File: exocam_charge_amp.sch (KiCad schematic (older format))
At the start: 8 parts, among them J1 dupont2x1, U1 TLV2771CDBVT

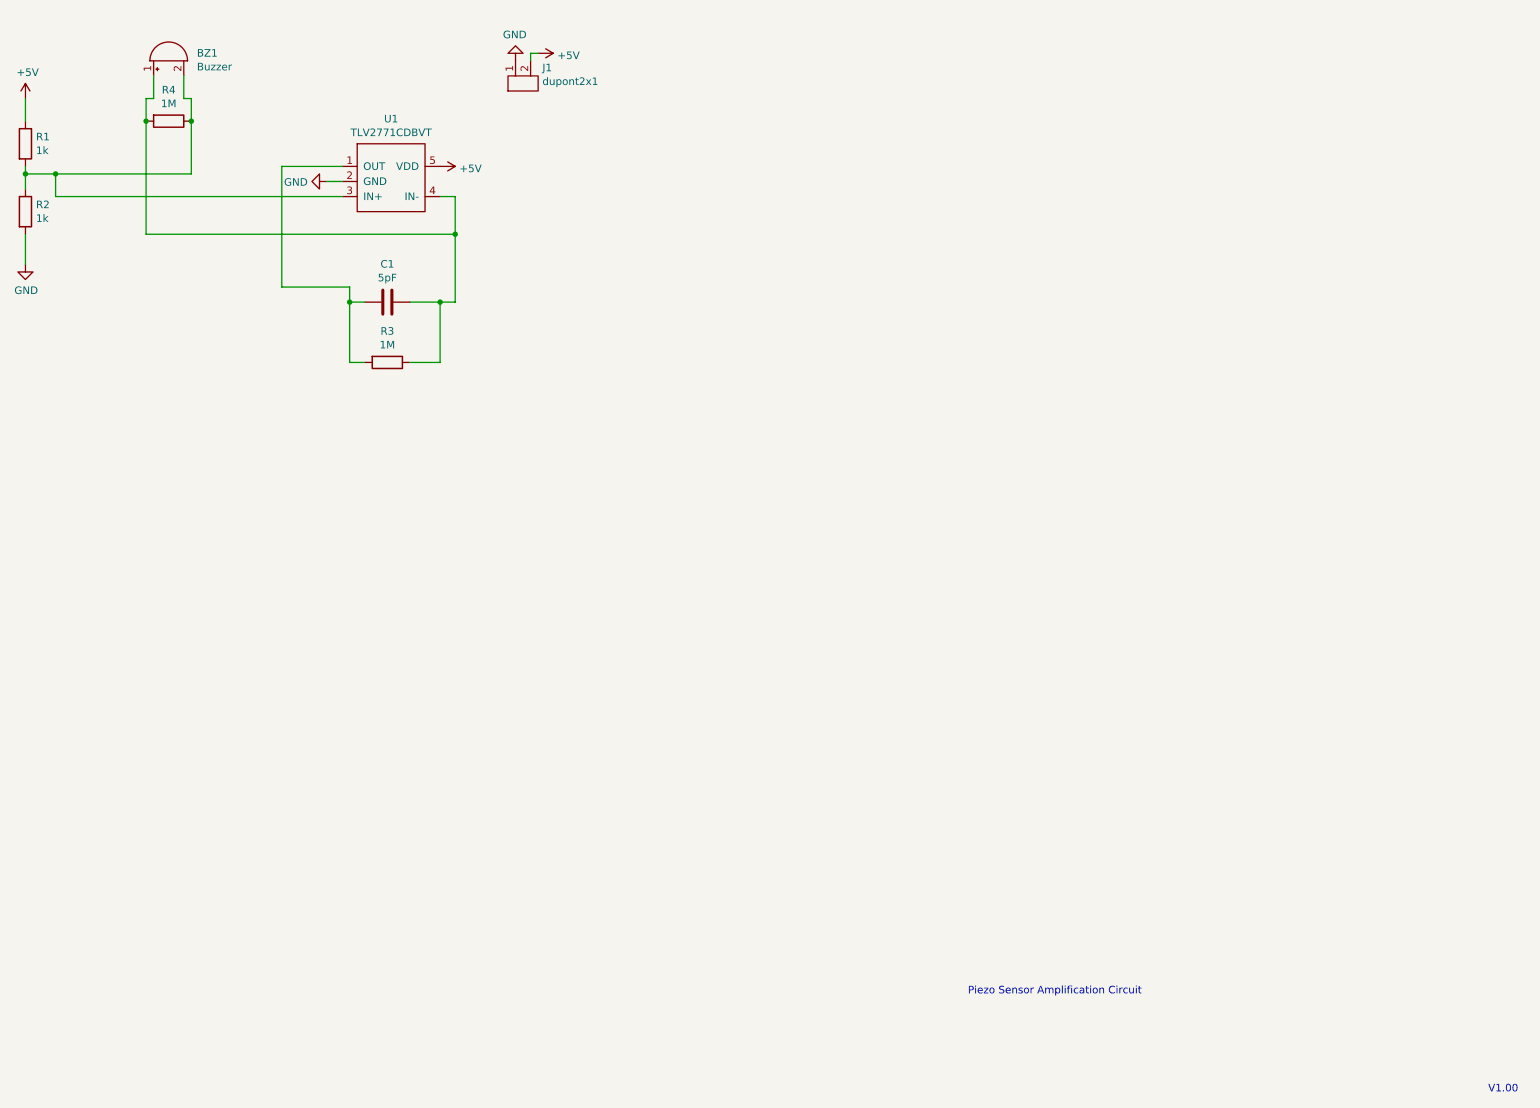
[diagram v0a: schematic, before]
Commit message: added step and updated to have screw mounts for the board
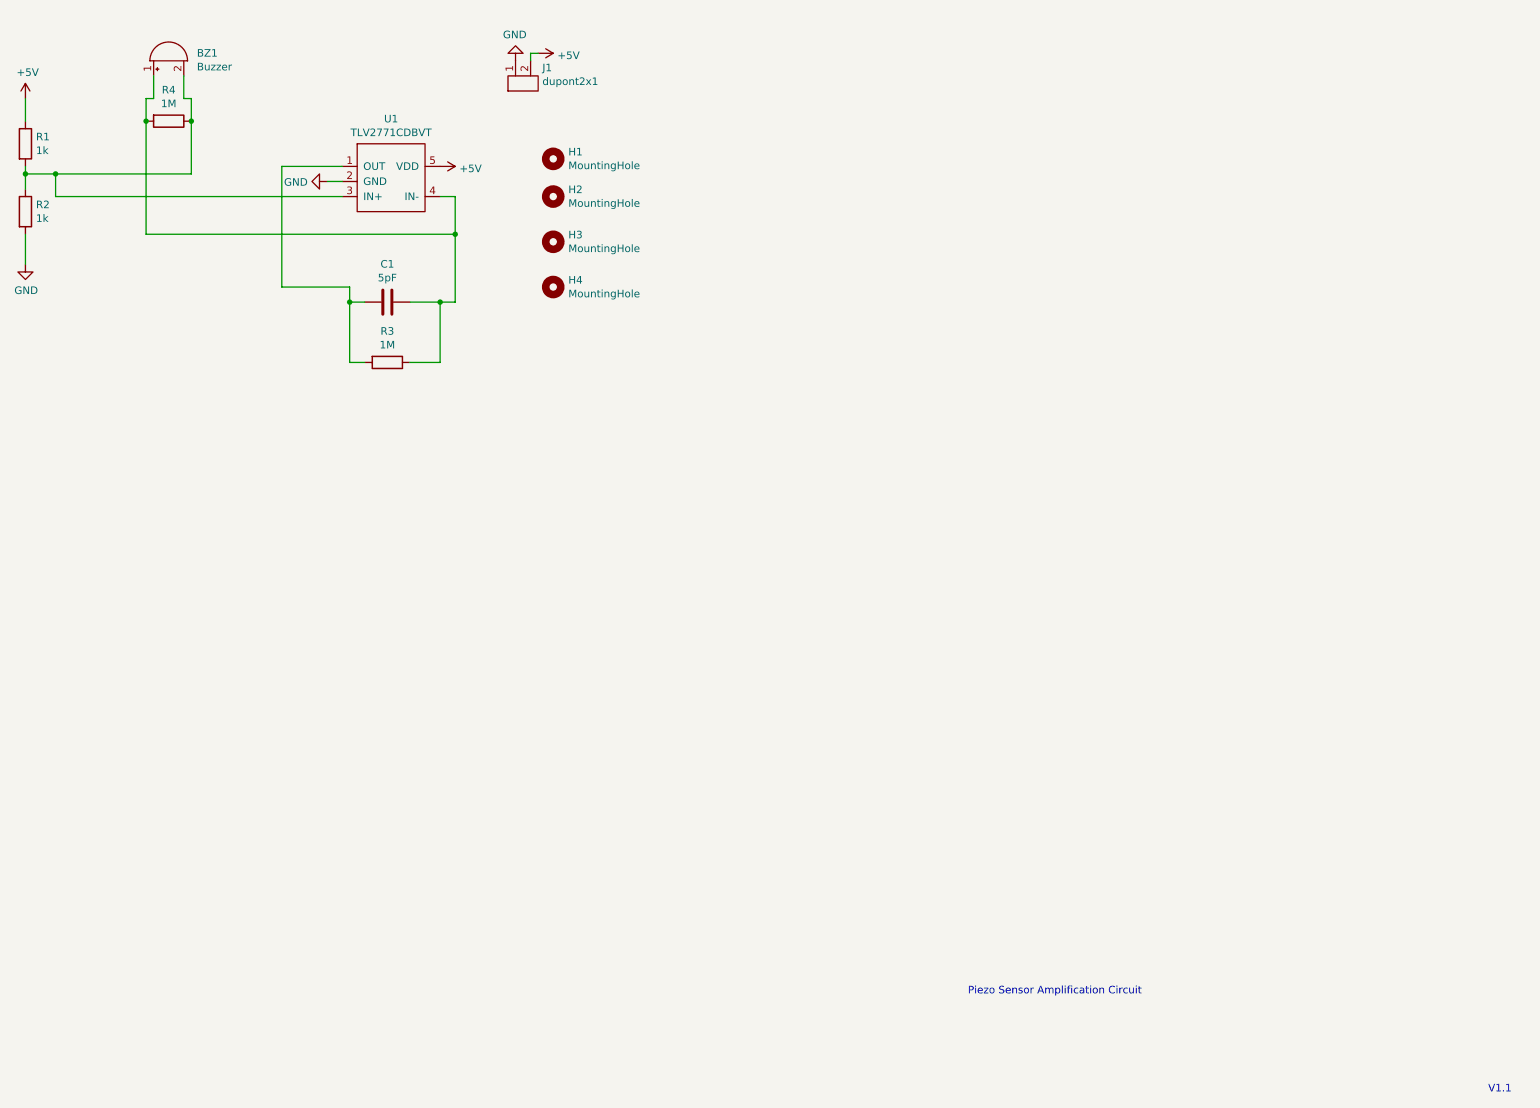
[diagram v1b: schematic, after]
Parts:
- added H1, H2, H3, H4: MountingHole, exocam_charge_amp:mount_hole_2.5mm, symbol Mechanical:MountingHole
- J1: footprint (none) -> exocam_charge_amp:dupont2x1
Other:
- note added: "V1.1\n"
- note removed: "V1.00\n"
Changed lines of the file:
@@
 Piezo Sensor Amplification Circuit
 Text Notes 10600 7650 0    50   ~ 0
-V1.00\n
+V1.1\n
 $Comp
 L exocam_charge_amp:TLV2771CDBVT U1
@@
 F 0 "J1" V 4154 672 50  0000 R CNN
 F 1 "dupont2x1" V 4063 672 50  0000 R CNN
-F 2 "" H 4050 1050 50  0001 C CNN
+F 2 "exocam_charge_amp:dupont2x1" H 4050 1050 50  0001 C CNN
 F 3 "" H 4050 1050 50  0001 C CNN
 	1    4100 900
@@
 $EndComp
 $Comp
-L power:GND #PWR?
+L power:GND #PWR0105
 U 1 1 60B84C12
 P 4150 800
-F 0 "#PWR?" H 4150 550 50  0001 C CNN
+F 0 "#PWR0105" H 4150 550 50  0001 C CNN
 F 1 "GND" H 4155 627 50  0000 C CNN
 F 2 "" H 4150 800 50  0001 C CNN
@@
 $EndComp
 $Comp
-L power:+5V #PWR?
+L power:+5V #PWR0106
 U 1 1 60B84E19
 P 4300 750
-F 0 "#PWR?" H 4300 600 50  0001 C CNN
+F 0 "#PWR0106" H 4300 600 50  0001 C CNN
 F 1 "+5V" V 4315 878 50  0000 L CNN
 F 2 "" H 4300 750 50  0001 C CNN
@@
 Wire Wire Line
 	1950 1050 1950 900
+$Comp
+L Mechanical:MountingHole H1
+U 1 1 60B97329
+P 4400 1450
+F 0 "H1" H 4500 1496 50  0000 L CNN
+F 1 "MountingHole" H 4500 1405 50  0000 L CNN
+F 2 "exocam_charge_amp:mount_hole_2.5mm" H 4400 1450 50  0001 C CNN
+F 3 "~" H 4400 1450 50  0001 C CNN
+	1    4400 1450
+	1    0    0    -1
+$EndComp
+$Comp
+L Mechanical:MountingHole H2
+U 1 1 60B9898F
+P 4400 1700
+F 0 "H2" H 4500 1746 50  0000 L CNN
+F 1 "MountingHole" H 4500 1655 50  0000 L CNN
+F 2 "exocam_charge_amp:mount_hole_2.5mm" H 4400 1700 50  0001 C CNN
+F 3 "~" H 4400 1700 50  0001 C CNN
+	1    4400 1700
+	1    0    0    -1
+$EndComp
+$Comp
+L Mechanical:MountingHole H3
+U 1 1 60B99095
+P 4400 2000
+F 0 "H3" H 4500 2046 50  0000 L CNN
+F 1 "MountingHole" H 4500 1955 50  0000 L CNN
+F 2 "exocam_charge_amp:mount_hole_2.5mm" H 4400 2000 50  0001 C CNN
+F 3 "~" H 4400 2000 50  0001 C CNN
+	1    4400 2000
+	1    0    0    -1
+$EndComp
+$Comp
+L Mechanical:MountingHole H4
+U 1 1 60B99959
+P 4400 2300
+F 0 "H4" H 4500 2346 50  0000 L CNN
+F 1 "MountingHole" H 4500 2255 50  0000 L CNN
+F 2 "exocam_charge_amp:mount_hole_2.5mm" H 4400 2300 50  0001 C CNN
+F 3 "~" H 4400 2300 50  0001 C CNN
+	1    4400 2300
+	1    0    0    -1
+$EndComp
 $EndSCHEMATC

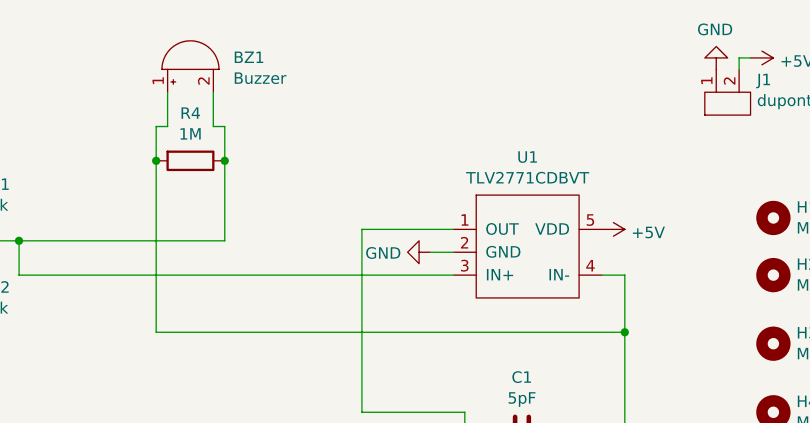
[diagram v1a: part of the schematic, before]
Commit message: added output terminals
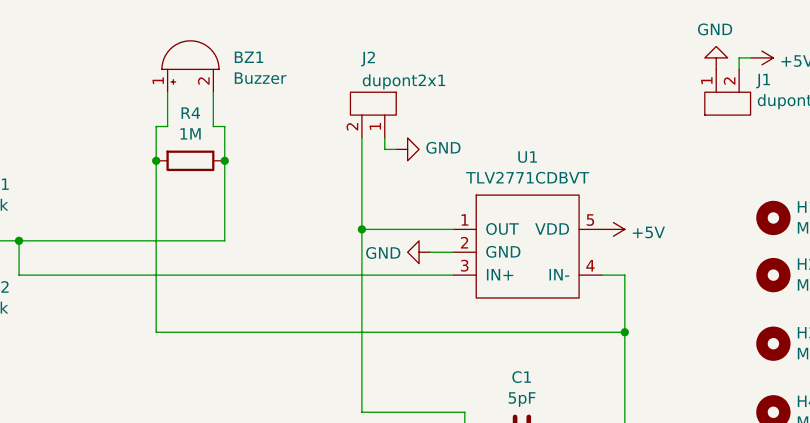
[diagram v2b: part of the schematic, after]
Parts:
- added J2: dupont2x1, exocam_charge_amp:dupont2x1, symbol exocam_charge_amp:dupont2x1
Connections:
- net GND: now also J2.1
- net at C1.2, R3.2, U1.1 (OUT): now also J2.2
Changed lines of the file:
@@
 	1    0    0    -1
 $EndComp
+$Comp
+L exocam_charge_amp:dupont2x1 J2
+U 1 1 60BB220E
+P 2750 1000
+F 0 "J2" V 2500 850 50  0000 L CNN
+F 1 "dupont2x1" V 2600 850 50  0000 L CNN
+F 2 "exocam_charge_amp:dupont2x1" H 2700 1150 50  0001 C CNN
+F 3 "" H 2700 1150 50  0001 C CNN
+	1    2750 1000
+	0    1    1    0
+$EndComp
+$Comp
+L power:GND #PWR?
+U 1 1 60BB5C21
+P 2750 1150
+F 0 "#PWR?" H 2750 900 50  0001 C CNN
+F 1 "GND" V 2755 1022 50  0000 R CNN
+F 2 "" H 2750 1150 50  0001 C CNN
+F 3 "" H 2750 1150 50  0001 C CNN
+	1    2750 1150
+	0    -1   -1   0
+$EndComp
+Wire Wire Line
+	2750 1150 2700 1150
+Wire Wire Line
+	2700 1150 2700 1100
+Wire Wire Line
+	2600 1100 2600 1500
+Connection ~ 2600 1500
 $EndSCHEMATC

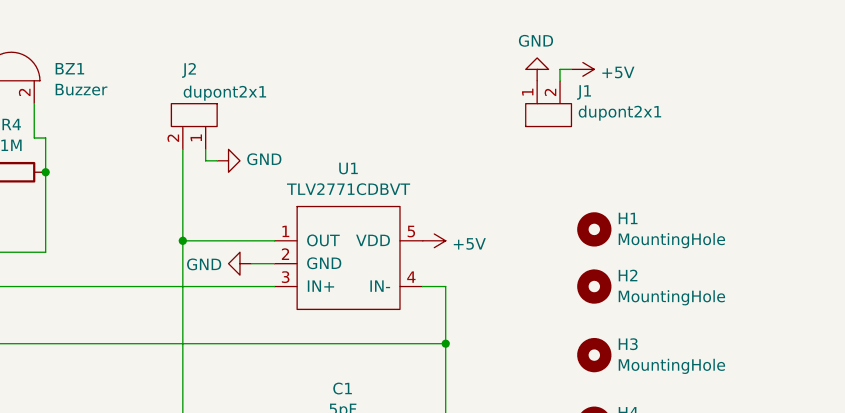
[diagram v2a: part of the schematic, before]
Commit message: updated pcb to be the new hole pattern on the shoulder side
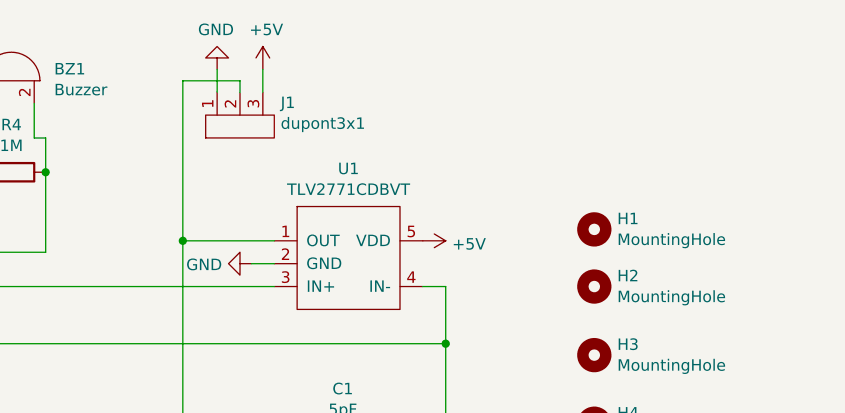
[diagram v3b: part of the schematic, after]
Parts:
- removed J1, J2: dupont2x1, exocam_charge_amp:dupont2x1, symbol exocam_charge_amp:dupont2x1
- added J1: dupont3x1, exocam_charge_amp:dupont3x1, symbol exocam_charge_amp:dupont3x1
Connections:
- net +5V: now also J1.3
- net GND: now also J1.1
- net at C1.2, R3.2, U1.1 (OUT): now also J1.2
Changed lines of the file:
@@
 	0    1    1    0
 $EndComp
-$Comp
-L exocam_charge_amp:dupont2x1 J1
-U 1 1 60B80DC6
-P 4100 900
-F 0 "J1" V 4154 672 50  0000 R CNN
-F 1 "dupont2x1" V 4063 672 50  0000 R CNN
-F 2 "exocam_charge_amp:dupont2x1" H 4050 1050 50  0001 C CNN
-F 3 "" H 4050 1050 50  0001 C CNN
-	1    4100 900
-	0    -1   -1   0
-$EndComp
-$Comp
-L power:GND #PWR0105
-U 1 1 60B84C12
-P 4150 800
-F 0 "#PWR0105" H 4150 550 50  0001 C CNN
-F 1 "GND" H 4155 627 50  0000 C CNN
-F 2 "" H 4150 800 50  0001 C CNN
-F 3 "" H 4150 800 50  0001 C CNN
-	1    4150 800
-	-1   0    0    1
-$EndComp
-$Comp
-L power:+5V #PWR0106
-U 1 1 60B84E19
-P 4300 750
-F 0 "#PWR0106" H 4300 600 50  0001 C CNN
-F 1 "+5V" V 4315 878 50  0000 L CNN
-F 2 "" H 4300 750 50  0001 C CNN
-F 3 "" H 4300 750 50  0001 C CNN
-	1    4300 750
-	0    1    1    0
-$EndComp
-Wire Wire Line
-	4250 750  4300 750
-Wire Wire Line
-	4250 800  4250 750
 Wire Wire Line
 	1750 1050 1750 900
@@
 $EndComp
 $Comp
-L exocam_charge_amp:dupont2x1 J2
-U 1 1 60BB220E
-P 2750 1000
-F 0 "J2" V 2500 850 50  0000 L CNN
-F 1 "dupont2x1" V 2600 850 50  0000 L CNN
-F 2 "exocam_charge_amp:dupont2x1" H 2700 1150 50  0001 C CNN
-F 3 "" H 2700 1150 50  0001 C CNN
-	1    2750 1000
-	0    1    1    0
+L exocam_charge_amp:dupont3x1 J1
+U 1 1 60DCA11E
+P 2700 950
+F 0 "J1" V 2754 622 50  0000 R CNN
+F 1 "dupont3x1" V 2663 622 50  0000 R CNN
+F 2 "exocam_charge_amp:dupont3x1" H 2650 1100 50  0001 C CNN
+F 3 "" H 2650 1100 50  0001 C CNN
+	1    2700 950
+	0    -1   -1   0
 $EndComp
 $Comp
 L power:GND #PWR?
-U 1 1 60BB5C21
-P 2750 1150
-F 0 "#PWR?" H 2750 900 50  0001 C CNN
-F 1 "GND" V 2755 1022 50  0000 R CNN
-F 2 "" H 2750 1150 50  0001 C CNN
-F 3 "" H 2750 1150 50  0001 C CNN
-	1    2750 1150
-	0    -1   -1   0
+U 1 1 60DCCF64
+P 2750 750
+F 0 "#PWR?" H 2750 500 50  0001 C CNN
+F 1 "GND" H 2755 577 50  0000 C CNN
+F 2 "" H 2750 750 50  0001 C CNN
+F 3 "" H 2750 750 50  0001 C CNN
+	1    2750 750
+	-1   0    0    1
 $EndComp
 Wire Wire Line
-	2750 1150 2700 1150
+	2750 850  2750 750
+$Comp
+L power:+5V #PWR?
+U 1 1 60DD0686
+P 2950 750
+F 0 "#PWR?" H 2950 600 50  0001 C CNN
+F 1 "+5V" H 2965 923 50  0000 C CNN
+F 2 "" H 2950 750 50  0001 C CNN
+F 3 "" H 2950 750 50  0001 C CNN
+	1    2950 750
+	1    0    0    -1
+$EndComp
 Wire Wire Line
-	2700 1150 2700 1100
+	2950 850  2950 750
 Wire Wire Line
-	2600 1100 2600 1500
+	2850 850  2850 800
+Wire Wire Line
+	2600 1500 2600 800
+Wire Wire Line
+	2600 800  2850 800
 Connection ~ 2600 1500
 $EndSCHEMATC

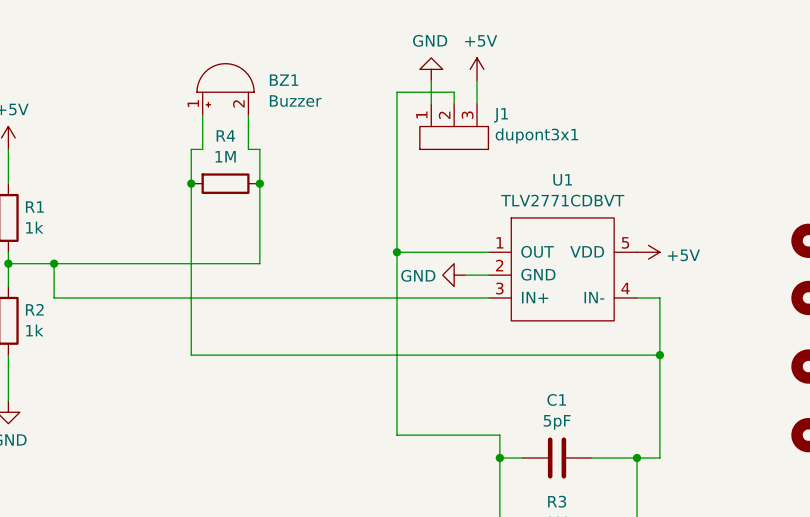
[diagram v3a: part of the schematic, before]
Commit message: modify board to be the two way amplification stage for higher range of outputs
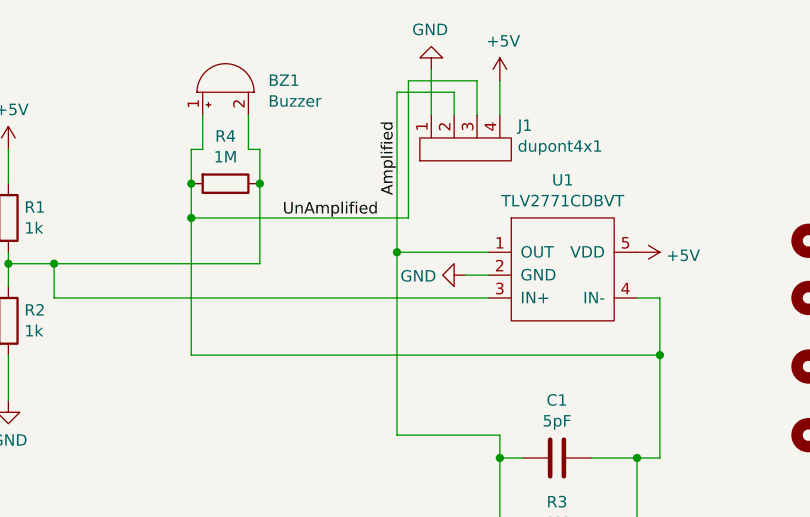
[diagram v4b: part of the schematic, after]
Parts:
- removed J1: dupont3x1, exocam_charge_amp:dupont3x1, symbol exocam_charge_amp:dupont3x1
- added J1: dupont4x1, exocam_charge_amp:dupont4x1, symbol exocam_charge_amp:dupont4x1
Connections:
- net +5V: now also J1.4
- net GND: now also J1.1
- net UnAmplified: now reaches BZ1.1 (-), C1.1, R3.1, R4.2, U1.4 (IN-)
- net UnAmplified: now also J1.3
- net Amplified: now reaches C1.2, R3.2, U1.1 (OUT)
- net Amplified: now also J1.2
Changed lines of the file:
@@
 	1700 1950 3750 1950
 Wire Wire Line
-	1700 1200 1700 1950
+	1700 1200 1700 1350
 Connection ~ 3750 1950
 Wire Wire Line
@@
 $EndComp
 $Comp
-L exocam_charge_amp:dupont3x1 J1
-U 1 1 60DCA11E
-P 2700 950
-F 0 "J1" V 2754 622 50  0000 R CNN
-F 1 "dupont3x1" V 2663 622 50  0000 R CNN
-F 2 "exocam_charge_amp:dupont3x1" H 2650 1100 50  0001 C CNN
-F 3 "" H 2650 1100 50  0001 C CNN
-	1    2700 950
-	0    -1   -1   0
+L power:GND #PWR0105
+U 1 1 60DCCF64
+P 2750 700
+F 0 "#PWR0105" H 2750 450 50  0001 C CNN
+F 1 "GND" H 2755 527 50  0000 C CNN
+F 2 "" H 2750 700 50  0001 C CNN
+F 3 "" H 2750 700 50  0001 C CNN
+	1    2750 700
+	-1   0    0    1
 $EndComp
 $Comp
-L power:GND #PWR?
-U 1 1 60DCCF64
-P 2750 750
-F 0 "#PWR?" H 2750 500 50  0001 C CNN
-F 1 "GND" H 2755 577 50  0000 C CNN
-F 2 "" H 2750 750 50  0001 C CNN
-F 3 "" H 2750 750 50  0001 C CNN
-	1    2750 750
-	-1   0    0    1
-$EndComp
-Wire Wire Line
-	2750 850  2750 750
-$Comp
-L power:+5V #PWR?
+L power:+5V #PWR0106
 U 1 1 60DD0686
-P 2950 750
-F 0 "#PWR?" H 2950 600 50  0001 C CNN
-F 1 "+5V" H 2965 923 50  0000 C CNN
-F 2 "" H 2950 750 50  0001 C CNN
-F 3 "" H 2950 750 50  0001 C CNN
-	1    2950 750
+P 3050 750
+F 0 "#PWR0106" H 3050 600 50  0001 C CNN
+F 1 "+5V" H 3065 923 50  0000 C CNN
+F 2 "" H 3050 750 50  0001 C CNN
+F 3 "" H 3050 750 50  0001 C CNN
+	1    3050 750
 	1    0    0    -1
 $EndComp
-Wire Wire Line
-	2950 850  2950 750
-Wire Wire Line
-	2850 850  2850 800
 Wire Wire Line
 	2600 1500 2600 800
@@
 	2600 800  2850 800
 Connection ~ 2600 1500
+$Comp
+L exocam_charge_amp:dupont4x1 J1
+U 1 1 60DF5917
+P 2700 1000
+F 0 "J1" V 2754 572 50  0000 R CNN
+F 1 "dupont4x1" V 2663 572 50  0000 R CNN
+F 2 "exocam_charge_amp:dupont4x1" H 2650 1150 50  0001 C CNN
+F 3 "" H 2650 1150 50  0001 C CNN
+	1    2700 1000
+	0    -1   -1   0
+$EndComp
+Wire Wire Line
+	3050 900  3050 750
+Wire Wire Line
+	2850 800  2850 900
+Wire Wire Line
+	2750 700  2750 900
+Wire Wire Line
+	1700 1350 2650 1350
+Wire Wire Line
+	2650 1350 2650 750
+Wire Wire Line
+	2650 750  2950 750
+Wire Wire Line
+	2950 750  2950 900
+Connection ~ 1700 1350
+Wire Wire Line
+	1700 1350 1700 1950
+Text Label 2100 1350 0    50   ~ 0
+UnAmplified
+Text Label 2600 1250 1    50   ~ 0
+Amplified
 $EndSCHEMATC

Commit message: updated so that vertical distance is correct for the holes
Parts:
- BZ1: symbol Device:Buzzer -> exocam_charge_amp-rescue:Buzzer-Device
- C1: symbol Device:C -> exocam_charge_amp-rescue:C-Device
- H1, H2, H3, H4: symbol Mechanical:MountingHole -> exocam_charge_amp-rescue:MountingHole-Mechanical
- R1, R2, R3, R4: symbol Device:R -> exocam_charge_amp-rescue:R-Device
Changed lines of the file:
@@
 $EndDescr
 $Comp
-L power:+5V #PWR0101
+L exocam_charge_amp-rescue:+5V-power #PWR0101
 U 1 1 60AC4579
 P 900 1050
@@
 $EndComp
 $Comp
-L Device:R R1
+L exocam_charge_amp-rescue:R-Device R1
 U 1 1 60AC52F9
 P 900 1350
@@
 $EndComp
 $Comp
-L Device:R R2
+L exocam_charge_amp-rescue:R-Device R2
 U 1 1 60AC57F6
 P 900 1800
@@
 	900  1950 900  2150
 $Comp
-L power:GND #PWR0102
+L exocam_charge_amp-rescue:GND-power #PWR0102
 U 1 1 60AC7448
 P 900 2150
@@
 $EndComp
 $Comp
-L Device:C C1
+L exocam_charge_amp-rescue:C-Device C1
 U 1 1 60AC9C31
 P 3300 2400
@@
 	3450 2400 3650 2400
 $Comp
-L Device:R R3
+L exocam_charge_amp-rescue:R-Device R3
 U 1 1 60ACB29B
 P 3300 2800
@@
 	3650 2800 3650 2400
 $Comp
-L Device:Buzzer BZ1
+L exocam_charge_amp-rescue:Buzzer-Device BZ1
 U 1 1 60AEB9E7
 P 1850 800
@@
 $EndComp
 $Comp
-L Device:R R4
+L exocam_charge_amp-rescue:R-Device R4
 U 1 1 60AECA35
 P 1850 1200
@@
 $EndComp
 $Comp
-L power:GND #PWR0103
+L exocam_charge_amp-rescue:GND-power #PWR0103
 U 1 1 60B68AE8
 P 2900 1600
@@
 	3750 1950 3750 2400
 $Comp
-L power:+5V #PWR0104
+L exocam_charge_amp-rescue:+5V-power #PWR0104
 U 1 1 60B6BDDA
 P 3650 1500
@@
 	1950 1050 1950 900
 $Comp
-L Mechanical:MountingHole H1
+L exocam_charge_amp-rescue:MountingHole-Mechanical H1
 U 1 1 60B97329
 P 4400 1450
@@
 $EndComp
 $Comp
-L Mechanical:MountingHole H2
+L exocam_charge_amp-rescue:MountingHole-Mechanical H2
 U 1 1 60B9898F
 P 4400 1700
@@
 $EndComp
 $Comp
-L Mechanical:MountingHole H3
+L exocam_charge_amp-rescue:MountingHole-Mechanical H3
 U 1 1 60B99095
 P 4400 2000
@@
 $EndComp
 $Comp
-L Mechanical:MountingHole H4
+L exocam_charge_amp-rescue:MountingHole-Mechanical H4
 U 1 1 60B99959
 P 4400 2300
@@
 $EndComp
 $Comp
-L power:GND #PWR0105
+L exocam_charge_amp-rescue:GND-power #PWR0105
 U 1 1 60DCCF64
 P 2750 700
@@
 $EndComp
 $Comp
-L power:+5V #PWR0106
+L exocam_charge_amp-rescue:+5V-power #PWR0106
 U 1 1 60DD0686
 P 3050 750
